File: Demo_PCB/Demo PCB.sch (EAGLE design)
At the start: 25 parts

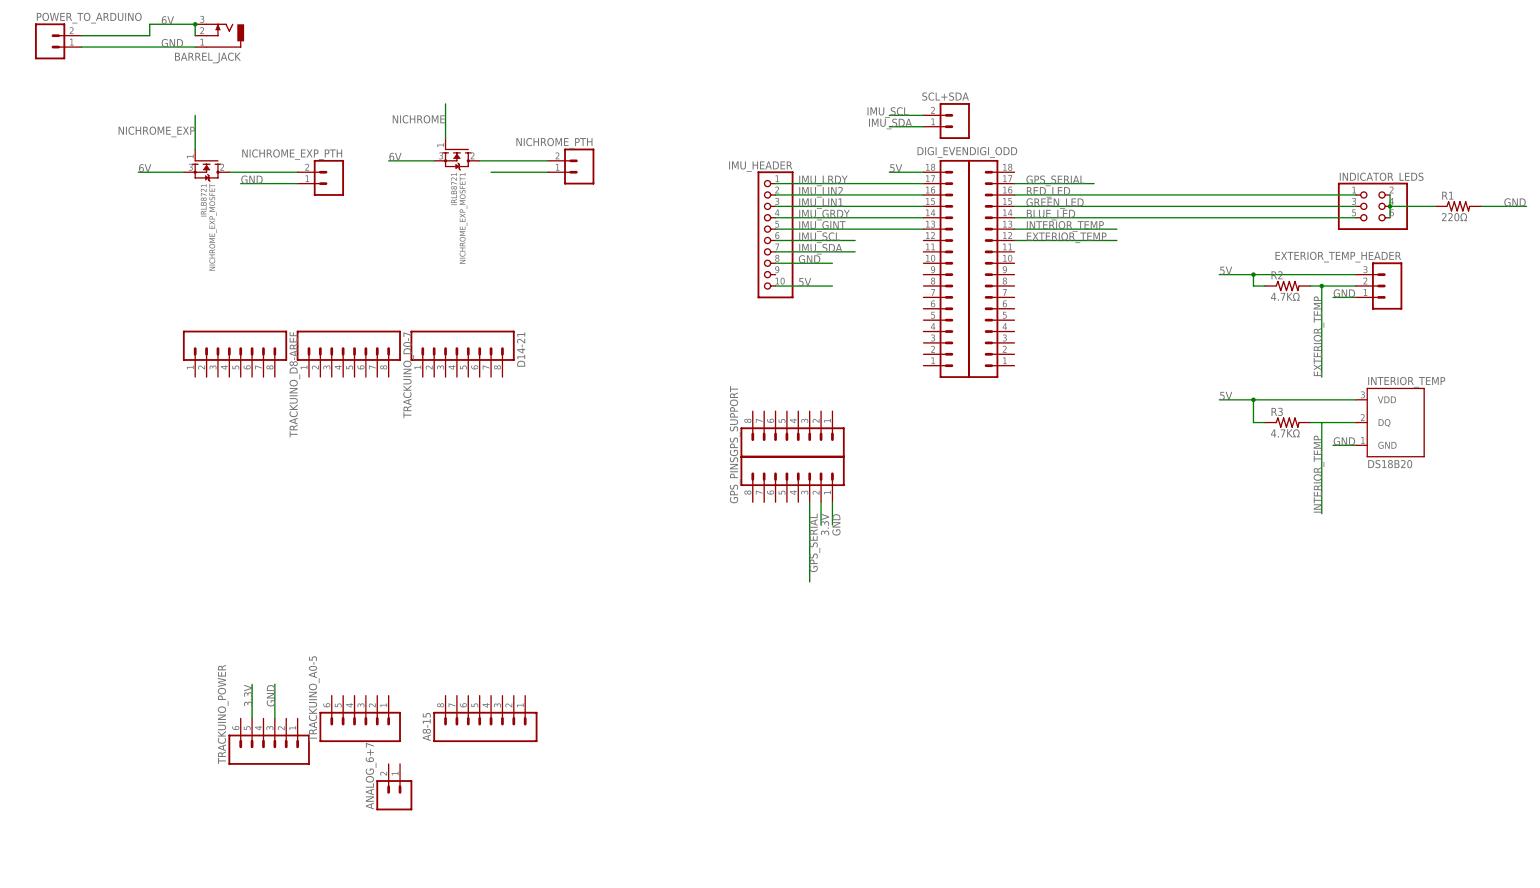
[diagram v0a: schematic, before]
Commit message: Add frame and title block to .sch, new idea for nichrome
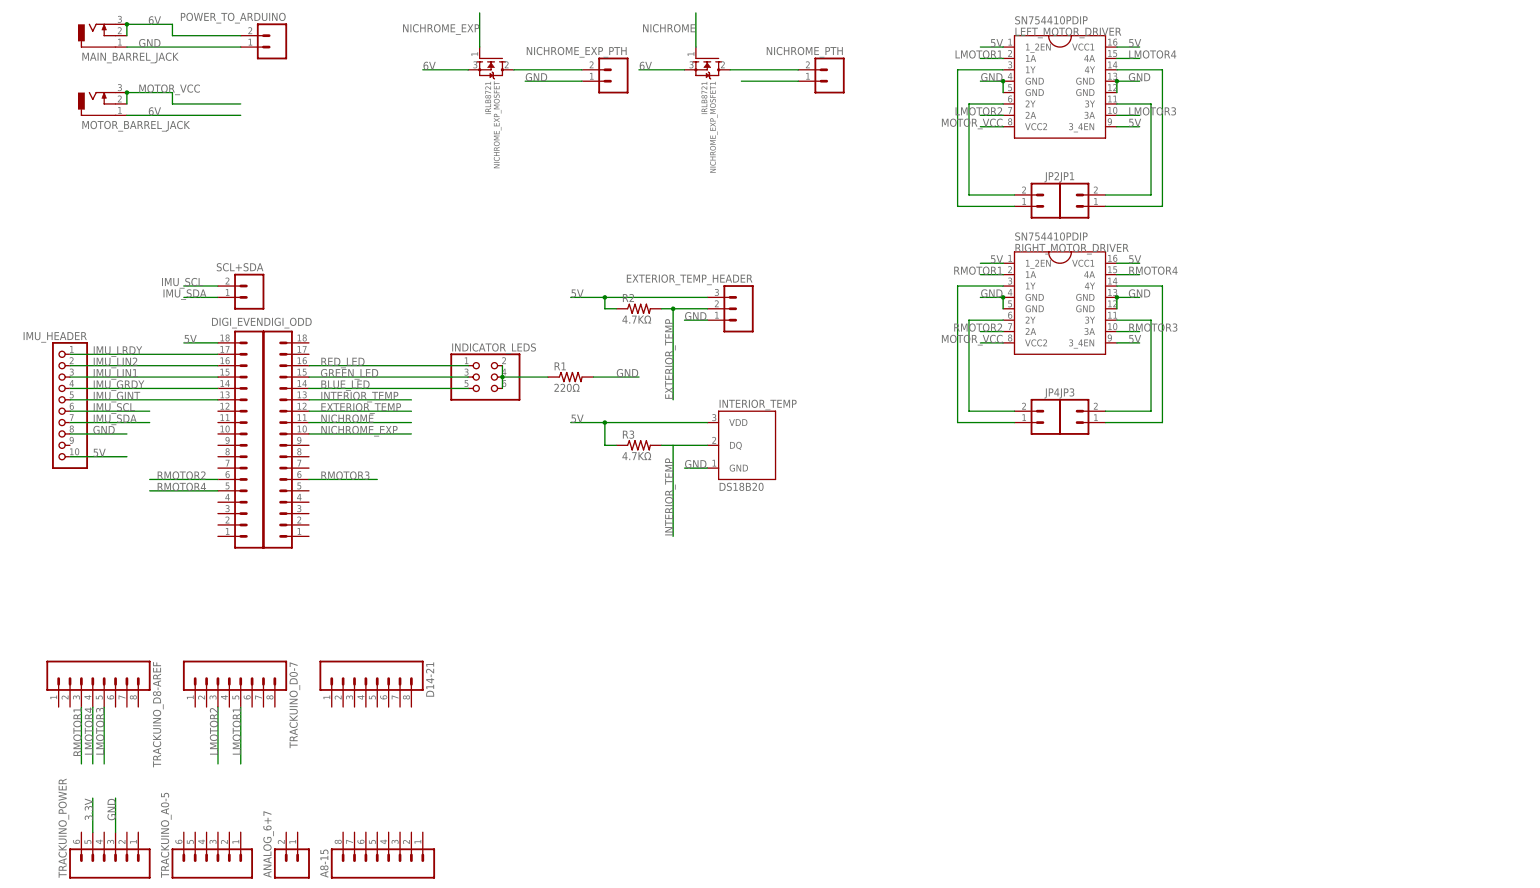
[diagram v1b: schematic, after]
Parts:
- removed BARREL_JACK: (no value), con-jack:DCJ0303
- removed GPS_PINS, GPS_SUPPORT: (no value), SparkFun-Connectors:M08
- added JP1, JP2, JP3, JP4: (no value), SparkFun-Connectors:M02PTH
- added LEFT_MOTOR_DRIVER, RIGHT_MOTOR_DRIVER: SN754410PDIP, AlexW-Eagle-Libraries:SN754410PDIP
- added MAIN_BARREL_JACK, MOTOR_BARREL_JACK: (no value), con-jack:DCJ0303
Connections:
- removed net GPS_SERIAL: DIGI_ODD.17, GPS_PINS.3
- new net LMOTOR1: LEFT_MOTOR_DRIVER.1A, TRACKUINO_D0-7.5
- new net LMOTOR2: LEFT_MOTOR_DRIVER.2A, TRACKUINO_D0-7.3
- new net LMOTOR3: LEFT_MOTOR_DRIVER.3A, TRACKUINO_D8-AREF.5
- new net LMOTOR4: LEFT_MOTOR_DRIVER.4A, TRACKUINO_D8-AREF.4
- new net MOTOR_VCC: LEFT_MOTOR_DRIVER.VCC2, MOTOR_BARREL_JACK.2, MOTOR_BARREL_JACK.3, RIGHT_MOTOR_DRIVER.VCC2
- new net N$10: JP4.2, RIGHT_MOTOR_DRIVER.2Y
- new net N$11: JP4.1, RIGHT_MOTOR_DRIVER.1Y
- new net N$3: JP1.2, LEFT_MOTOR_DRIVER.3Y
- new net N$4: JP1.1, LEFT_MOTOR_DRIVER.4Y
- new net N$6: JP2.2, LEFT_MOTOR_DRIVER.2Y
- new net N$7: JP2.1, LEFT_MOTOR_DRIVER.1Y
- new net N$8: JP3.2, RIGHT_MOTOR_DRIVER.3Y
- new net N$9: JP3.1, RIGHT_MOTOR_DRIVER.4Y
- new net NICHROME: DIGI_ODD.11, NICHROME_EXP_MOSFET1.G
- new net RMOTOR1: RIGHT_MOTOR_DRIVER.1A, TRACKUINO_D8-AREF.3
- new net RMOTOR2: DIGI_EVEN.6, RIGHT_MOTOR_DRIVER.2A
- new net RMOTOR3: DIGI_ODD.6, RIGHT_MOTOR_DRIVER.3A
- new net RMOTOR4: DIGI_EVEN.5, RIGHT_MOTOR_DRIVER.4A
- net 3.3V: no longer GPS_PINS.2
- net 5V: now also LEFT_MOTOR_DRIVER.1_2EN, LEFT_MOTOR_DRIVER.3_4EN, LEFT_MOTOR_DRIVER.VCC1, RIGHT_MOTOR_DRIVER.1_2EN, RIGHT_MOTOR_DRIVER.3_4EN, RIGHT_MOTOR_DRIVER.VCC1
- net 6V: now also MAIN_BARREL_JACK.2, MAIN_BARREL_JACK.3, MOTOR_BARREL_JACK.1, NICHROME_EXP_MOSFET1.S; no longer BARREL_JACK.2, BARREL_JACK.3
- net GND: now also LEFT_MOTOR_DRIVER.GND@1, LEFT_MOTOR_DRIVER.GND@2, LEFT_MOTOR_DRIVER.GND@3, LEFT_MOTOR_DRIVER.GND@4, MAIN_BARREL_JACK.1, RIGHT_MOTOR_DRIVER.GND@1, RIGHT_MOTOR_DRIVER.GND@2, RIGHT_MOTOR_DRIVER.GND@3, RIGHT_MOTOR_DRIVER.GND@4; no longer BARREL_JACK.1, GPS_PINS.1
- net NICHROME_EXP: now also DIGI_ODD.10
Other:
- moved on the sheet: A8-15, ANALOG_6+7, D14-21, DIGI_EVEN, DIGI_ODD, EXTERIOR_TEMP_HEADER, IMU_HEADER, INDICATOR_LEDS, INTERIOR_TEMP, NICHROME_EXP_MOSFET, NICHROME_EXP_MOSFET1, NICHROME_EXP_PTH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

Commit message: Change MOSFETS to Relays + Finalize Board
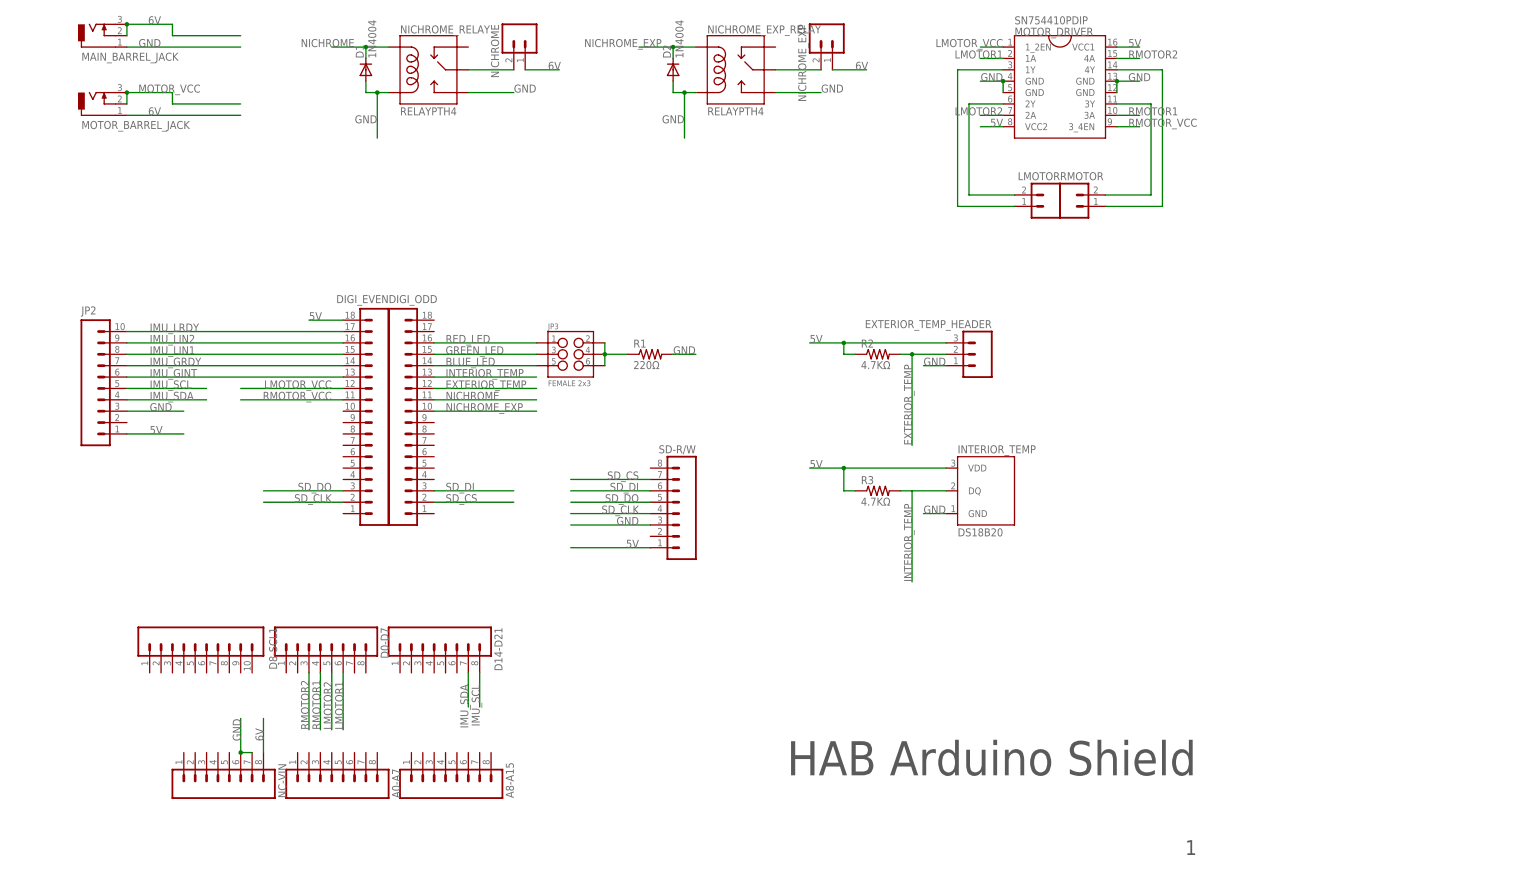
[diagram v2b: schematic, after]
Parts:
- removed A8-15, D14-21, TRACKUINO_D0-7, TRACKUINO_D8-AREF: (no value), SparkFun-Connectors:M08
- removed ANALOG_6+7, JP4, NICHROME_EXP_PTH, NICHROME_PTH, POWER_TO_ARDUINO, SCL+SDA: (no value), SparkFun-Connectors:M02PTH
- removed IMU_HEADER: (no value), pinhead:PINHD-1X10
- removed INDICATOR_LEDS: (no value), pinhead:PINHD-2X3
- removed NICHROME_EXP_MOSFET, NICHROME_EXP_MOSFET1: IRLB8721, adafruit:MOSFET-NGDS_TO220V
- removed RIGHT_MOTOR_DRIVER: SN754410PDIP, AlexW-Eagle-Libraries:SN754410PDIP
- removed TRACKUINO_A0-5, TRACKUINO_POWER: (no value), SparkFun-Connectors:M06SILK_FEMALE_PTH
- added A0-A7, A8-A15, D0-D7, D14-D21, NC-VIN, SD-R/W: (no value), SparkFun-Connectors:M08
- added D1, D2: 1N4004, adafruit:1N4004
- added D8-SCL1: (no value), SparkFun-Connectors:M10SILK_FEMALE_PTH
- added LMOTOR, NICHROME, NICHROME_EXP: (no value), SparkFun-Connectors:M02PTH
- added NICHROME_EXP_RELAY, NICHROME_RELAY: RELAYPTH4, SparkFun-Electromechanical:RELAYPTH4
- JP2: device SparkFun-Connectors:M02PTH -> SparkFun-Connectors:M10SILK_FEMALE_PTH
- JP3: value (none) -> FEMALE 2x3; device SparkFun-Connectors:M02PTH -> SparkFun-Connectors:M03X2FEMALE
- renumbered JP1 to RMOTOR, LEFT_MOTOR_DRIVER to MOTOR_DRIVER
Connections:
- removed net 3.3V: TRACKUINO_POWER.5
- removed net LMOTOR3: MOTOR_DRIVER.3A, TRACKUINO_D8-AREF.5
- removed net LMOTOR4: MOTOR_DRIVER.4A, TRACKUINO_D8-AREF.4
- removed net N$10: JP4.2, RIGHT_MOTOR_DRIVER.2Y
- removed net N$11: JP4.1, RIGHT_MOTOR_DRIVER.1Y
- removed net N$8: JP3.2, RIGHT_MOTOR_DRIVER.3Y
- removed net N$9: JP3.1, RIGHT_MOTOR_DRIVER.4Y
- removed net RMOTOR3: DIGI_ODD.6, RIGHT_MOTOR_DRIVER.3A
- removed net RMOTOR4: DIGI_EVEN.5, RIGHT_MOTOR_DRIVER.4A
- new net LMOTOR_VCC: DIGI_EVEN.12, MOTOR_DRIVER.1_2EN
- new net N$14: NICHROME.2, NICHROME_RELAY.MAIN
- new net RMOTOR_VCC: DIGI_EVEN.11, MOTOR_DRIVER.3_4EN
- new net SD_CLK: DIGI_EVEN.2, SD-R/W.4
- new net SD_CS: DIGI_ODD.2, SD-R/W.7
- new net SD_DI: DIGI_ODD.3, SD-R/W.6
- new net SD_DO: DIGI_EVEN.3, SD-R/W.5
- net 5V: now also JP2.1, MOTOR_DRIVER.VCC2, SD-R/W.1; no longer IMU_HEADER.10, MOTOR_DRIVER.1_2EN, MOTOR_DRIVER.3_4EN, RIGHT_MOTOR_DRIVER.1_2EN, RIGHT_MOTOR_DRIVER.3_4EN, RIGHT_MOTOR_DRIVER.VCC1
- net 6V: now also NC-VIN.8, NICHROME.1, NICHROME_EXP.1; no longer NICHROME_EXP_MOSFET.S, NICHROME_EXP_MOSFET1.S, POWER_TO_ARDUINO.2
- net BLUE_LED: now also JP3.5; no longer INDICATOR_LEDS.5
- net GND: now also D1.A, D2.A, JP2.3, NC-VIN.6, NC-VIN.7, NICHROME_EXP_RELAY.COIL2, NICHROME_EXP_RELAY.NO, NICHROME_RELAY.COIL2, NICHROME_RELAY.NO, SD-R/W.3; no longer IMU_HEADER.8, NICHROME_EXP_PTH.1, NICHROME_PTH.1, POWER_TO_ARDUINO.1, RIGHT_MOTOR_DRIVER.GND@1, RIGHT_MOTOR_DRIVER.GND@2, RIGHT_MOTOR_DRIVER.GND@3, RIGHT_MOTOR_DRIVER.GND@4, TRACKUINO_POWER.3
- net GREEN_LED: now also JP3.3; no longer INDICATOR_LEDS.3
- net IMU_GINT: now also JP2.6; no longer IMU_HEADER.5
- net IMU_GRDY: now also JP2.7; no longer IMU_HEADER.4
- net IMU_LIN1: now also JP2.8; no longer IMU_HEADER.3
- net IMU_LIN2: now also JP2.9; no longer IMU_HEADER.2
- net IMU_LRDY: now also JP2.10; no longer IMU_HEADER.1
- net IMU_SCL: now also D14-D21.8, JP2.5; no longer IMU_HEADER.6, SCL+SDA.2
- net IMU_SDA: now also D14-D21.7, JP2.4; no longer IMU_HEADER.7, SCL+SDA.1
- net LMOTOR1: now also D0-D7.6; no longer TRACKUINO_D0-7.5
- net LMOTOR2: now also D0-D7.5; no longer TRACKUINO_D0-7.3
- net MOTOR_VCC: no longer MOTOR_DRIVER.VCC2, RIGHT_MOTOR_DRIVER.VCC2
- net N$2: now also NICHROME_EXP.2, NICHROME_EXP_RELAY.MAIN; no longer NICHROME_EXP_MOSFET.D, NICHROME_EXP_MOSFET1.D, NICHROME_EXP_PTH.2, NICHROME_PTH.2
- net N$5: now also JP3.2, JP3.4, JP3.6; no longer INDICATOR_LEDS.2, INDICATOR_LEDS.4, INDICATOR_LEDS.6
- net N$6: now also LMOTOR.2; no longer JP2.2
- net N$7: now also LMOTOR.1; no longer JP2.1
- net NICHROME: now also D1.C, NICHROME_RELAY.COIL1; no longer NICHROME_EXP_MOSFET1.G
- net NICHROME_EXP: now also D2.C, NICHROME_EXP_RELAY.COIL1; no longer NICHROME_EXP_MOSFET.G
- net RED_LED: now also JP3.1; no longer INDICATOR_LEDS.1
- net RMOTOR1: now also D0-D7.4, MOTOR_DRIVER.3A; no longer RIGHT_MOTOR_DRIVER.1A, TRACKUINO_D8-AREF.3
- net RMOTOR2: now also D0-D7.3, MOTOR_DRIVER.4A; no longer DIGI_EVEN.6, RIGHT_MOTOR_DRIVER.2A
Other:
- note added: "1"
- note added: "HAB Arduino Shield"
- moved on the sheet: DIGI_EVEN, DIGI_ODD, EXTERIOR_TEMP_HEADER, INTERIOR_TEMP, R1, R2, R3
